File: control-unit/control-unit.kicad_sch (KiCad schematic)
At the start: 23 parts

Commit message: Moved wires to more easily do operating point analysis
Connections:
- net D2 is gone; now on net +5V: D2.1 (Pin_1)
- net D3 is gone; now on net +5V: D3.1 (Pin_1)
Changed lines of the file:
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@@
+	)
+	(junction
+		(at 46.99 58.42)
+		(diameter 0)
+		(color 0 0 0 0)
 	)
 	(junction
@@
 	)
 	(junction
+		(at 46.99 68.58)
+		(diameter 0)
+		(color 0 0 0 0)
+	)
+	(junction
 		(at 228.6 92.71)
 		(diameter 0)
@@
 	(wire
 		(pts
+			(xy 74.93 78.74) (xy 67.31 78.74)
+		)
+		(stroke
+			(width 0)
+			(type default)
+		)
+	)
+	(wire
+		(pts
 			(xy 50.8 58.42) (xy 54.61 58.42)
 		)
@@
 	(wire
 		(pts
+			(xy 67.31 48.26) (xy 74.93 48.26)
+		)
+		(stroke
+			(width 0)
+			(type default)
+		)
+	)
+	(wire
+		(pts
 			(xy 50.8 44.45) (xy 50.8 48.26)
 		)
@@
 	(wire
 		(pts
+			(xy 46.99 67.31) (xy 46.99 68.58)
+		)
+		(stroke
+			(width 0)
+			(type default)
+		)
+	)
+	(wire
+		(pts
 			(xy 222.25 138.43) (xy 207.01 138.43)
 		)
@@
 	(wire
 		(pts
+			(xy 74.93 58.42) (xy 67.31 58.42)
+		)
+		(stroke
+			(width 0)
+			(type default)
+		)
+	)
+	(wire
+		(pts
 			(xy 193.04 101.6) (xy 193.04 110.49)
 		)
@@
 		(pts
 			(xy 46.99 48.26) (xy 50.8 48.26)
+		)
+		(stroke
+			(width 0)
+			(type default)
+		)
+	)
+	(wire
+		(pts
+			(xy 74.93 68.58) (xy 67.31 68.58)
 		)
 		(stroke
@@
 	)
 	(label "NOT_D1"
-		(at 67.31 48.26 0)
+		(at 74.93 48.26 0)
 		(fields_autoplaced yes)
 		(effects
@@
 	)
 	(label "NOT_D3"
-		(at 67.31 68.58 0)
+		(at 74.93 68.58 0)
 		(fields_autoplaced yes)
 		(effects
@@
 	)
 	(label "NOT_D2"
-		(at 67.31 58.42 0)
+		(at 74.93 58.42 0)
 		(fields_autoplaced yes)
 		(effects
@@
 	)
 	(label "NOT_D4"
-		(at 67.31 78.74 0)
+		(at 74.93 78.74 0)
 		(fields_autoplaced yes)
 		(effects
@@
 	)
 	(symbol
+		(lib_id "power:+5V")
+		(at 46.99 67.31 0)
+		(unit 1)
+		(exclude_from_sim no)
+		(in_bom yes)
+		(on_board yes)
+		(dnp no)
+		(fields_autoplaced yes)
+		(property "Reference" "#PWR0124"
+			(at 46.99 71.12 0)
+			(effects
+				(font
+					(size 1.27 1.27)
+				)
+				(hide yes)
+			)
+		)
+		(property "Value" "+5V"
+			(at 46.99 62.23 0)
+			(effects
+				(font
+					(size 1.27 1.27)
+				)
+			)
+		)
+		(property "Footprint" ""
+			(at 46.99 67.31 0)
+			(effects
+				(font
+					(size 1.27 1.27)
+				)
+				(hide yes)
+			)
+		)
+		(property "Datasheet" ""
+			(at 46.99 67.31 0)
+			(effects
+				(font
+					(size 1.27 1.27)
+				)
+				(hide yes)
+			)
+		)
+		(property "Description" "Power symbol creates a global label with name \"+5V\""
+			(at 46.99 67.31 0)
+			(effects
+				(font
+					(size 1.27 1.27)
+				)
+				(hide yes)
+			)
+		)
+		(pin "1"
+		)
+		(instances
+			(project ""
+				(path "/1cf3a7ee-ec47-45b6-b515-1840d726ab8f"
+					(reference "#PWR0124")
+					(unit 1)
+				)
+			)
+		)
+	)
+	(symbol
 		(lib_id "Connector_Generic:Conn_01x01")
 		(at 262.89 80.01 0)
@@
 					(unit 1)
 				)
+			)
+		)
+	)
+	(symbol
+		(lib_id "power:+5V")
+		(at 46.99 58.42 0)
+		(unit 1)
+		(exclude_from_sim no)
+		(in_bom yes)
+		(on_board yes)
+		(dnp no)
+		(fields_autoplaced yes)
+		(property "Reference" "#PWR0125"
+			(at 46.99 62.23 0)
+			(effects
+				(font
+					(size 1.27 1.27)
+				)
+				(hide yes)
+			)
+		)
+		(property "Value" "+5V"
+			(at 46.99 53.34 0)
+			(effects
+				(font
+					(size 1.27 1.27)
+				)
+			)
+		)
+		(property "Footprint" ""
+			(at 46.99 58.42 0)
+			(effects
+				(font
+					(size 1.27 1.27)
+				)
+				(hide yes)
+			)
+		)
+		(property "Datasheet" ""
+			(at 46.99 58.42 0)
+			(effects
+				(font
+					(size 1.27 1.27)
+				)
+				(hide yes)
+			)
+		)
+		(property "Description" "Power symbol creates a global label with name \"+5V\""
+			(at 46.99 58.42 0)
+			(effects
+				(font
+					(size 1.27 1.27)
+				)
+				(hide yes)
+			)
+		)
+		(pin "1"
+		)
+		(instances
+			(project "control-unit"
+				(path "/1cf3a7ee-ec47-45b6-b515-1840d726ab8f"
+					(reference "#PWR0125")
+					(unit 1)
+				)

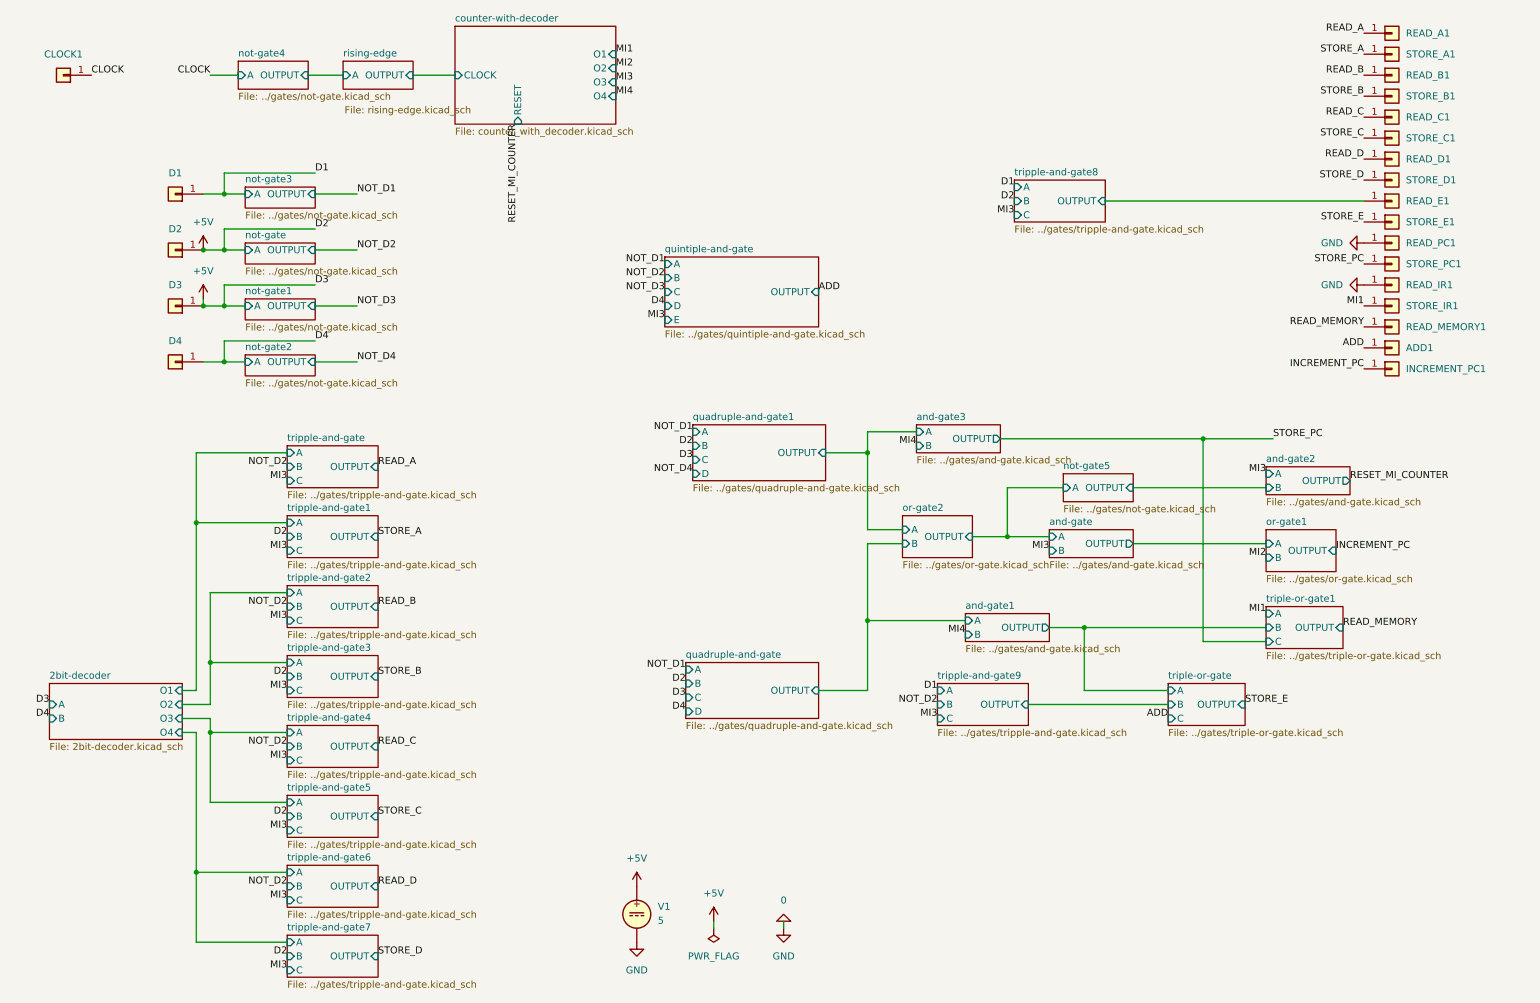
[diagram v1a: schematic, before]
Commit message: Use IC circuits in adder circuit
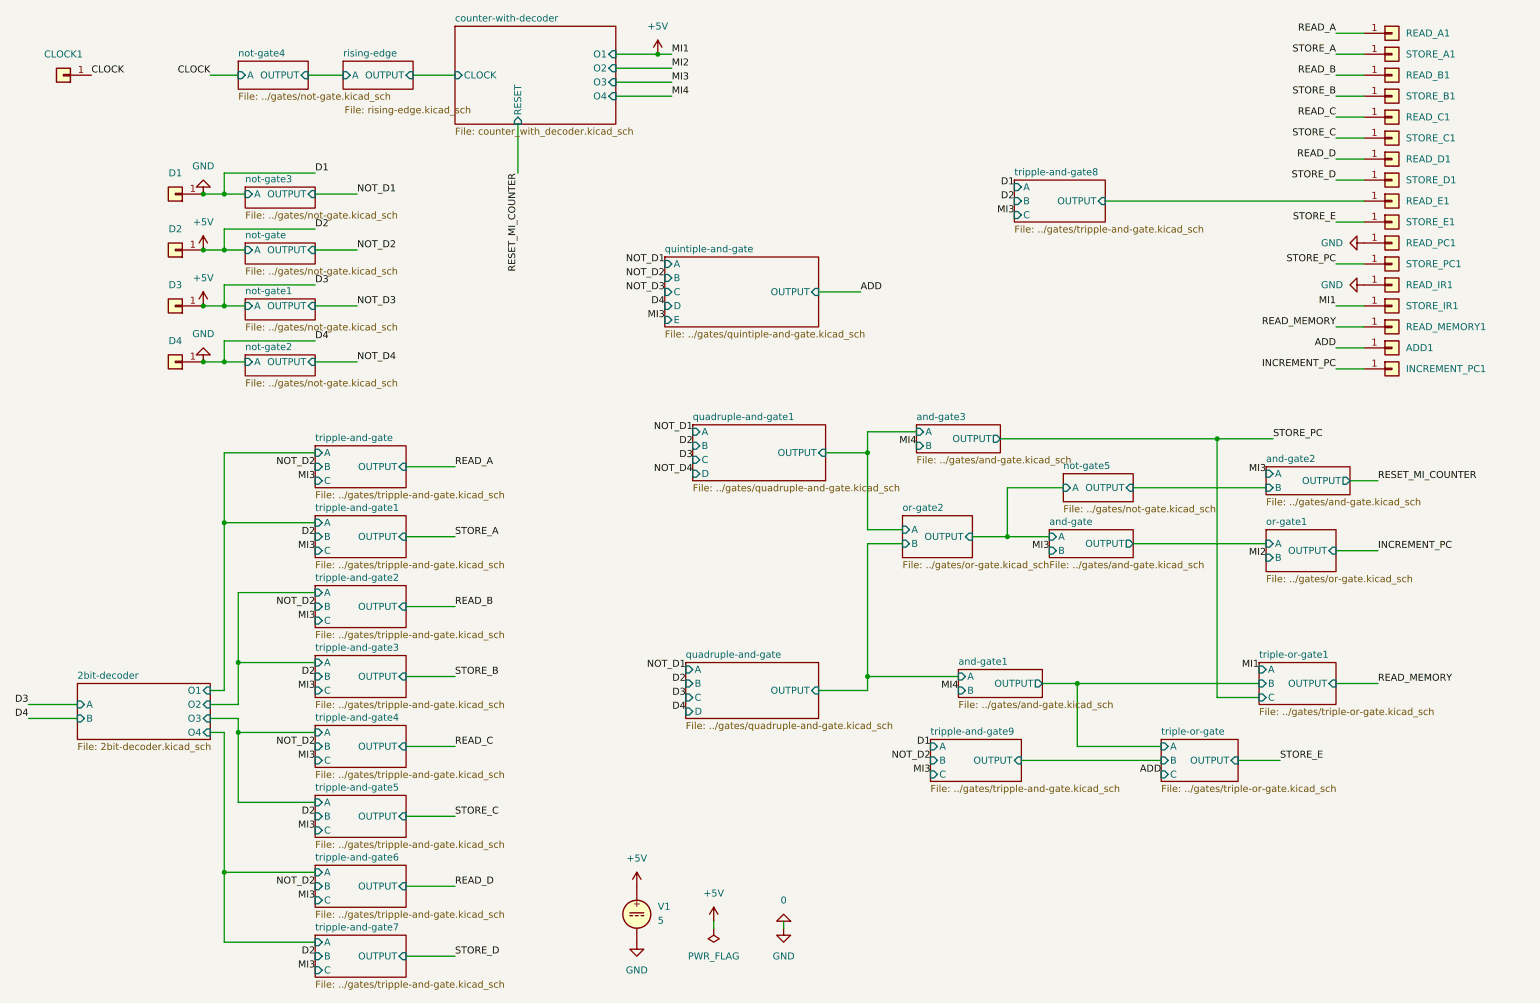
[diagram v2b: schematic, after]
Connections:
- net D1 is gone; now on net 0: D1.1 (Pin_1)
- net D4 is gone; now on net 0: D4.1 (Pin_1)
- net MI1 is gone; now on net +5V: STORE_IR1.1 (Pin_1)
